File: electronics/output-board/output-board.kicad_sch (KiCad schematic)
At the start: 27 parts, among them J14 Arming switch, J19 Extra IO, J3 12V In, J4 Conn_01x02, J5 SWD Header, J6 Conn_01x02, SW1 SW_Push_Dual, U1 MAX33012EASA+, U2 LD3985M33R_SOT23, U3 STM32F105VBH6, Y1 25MHz 9pF

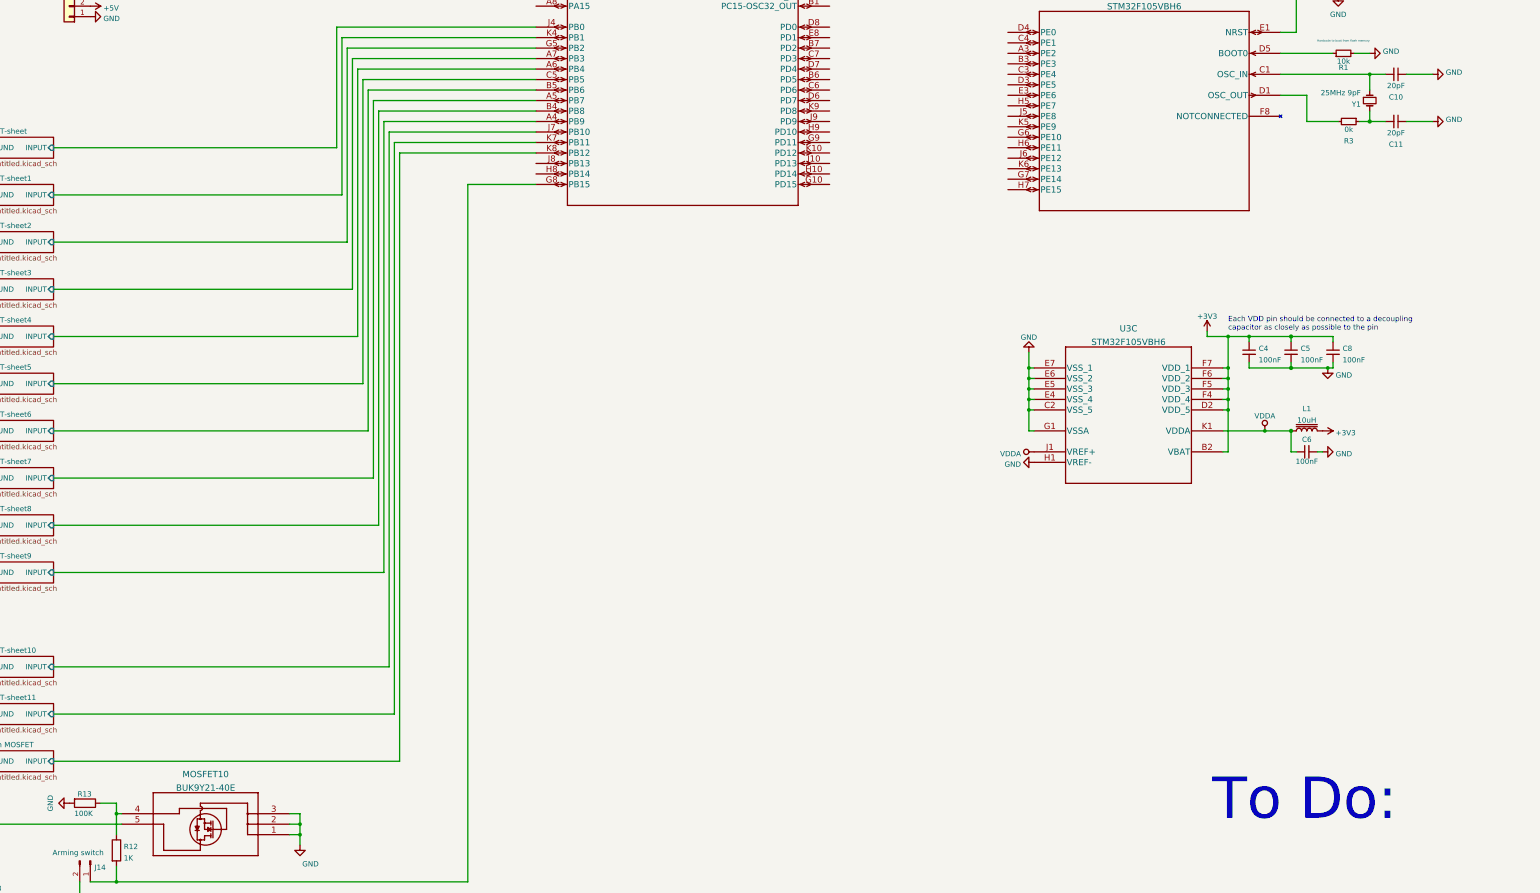
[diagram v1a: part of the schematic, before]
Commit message: continued working on four-layer output board
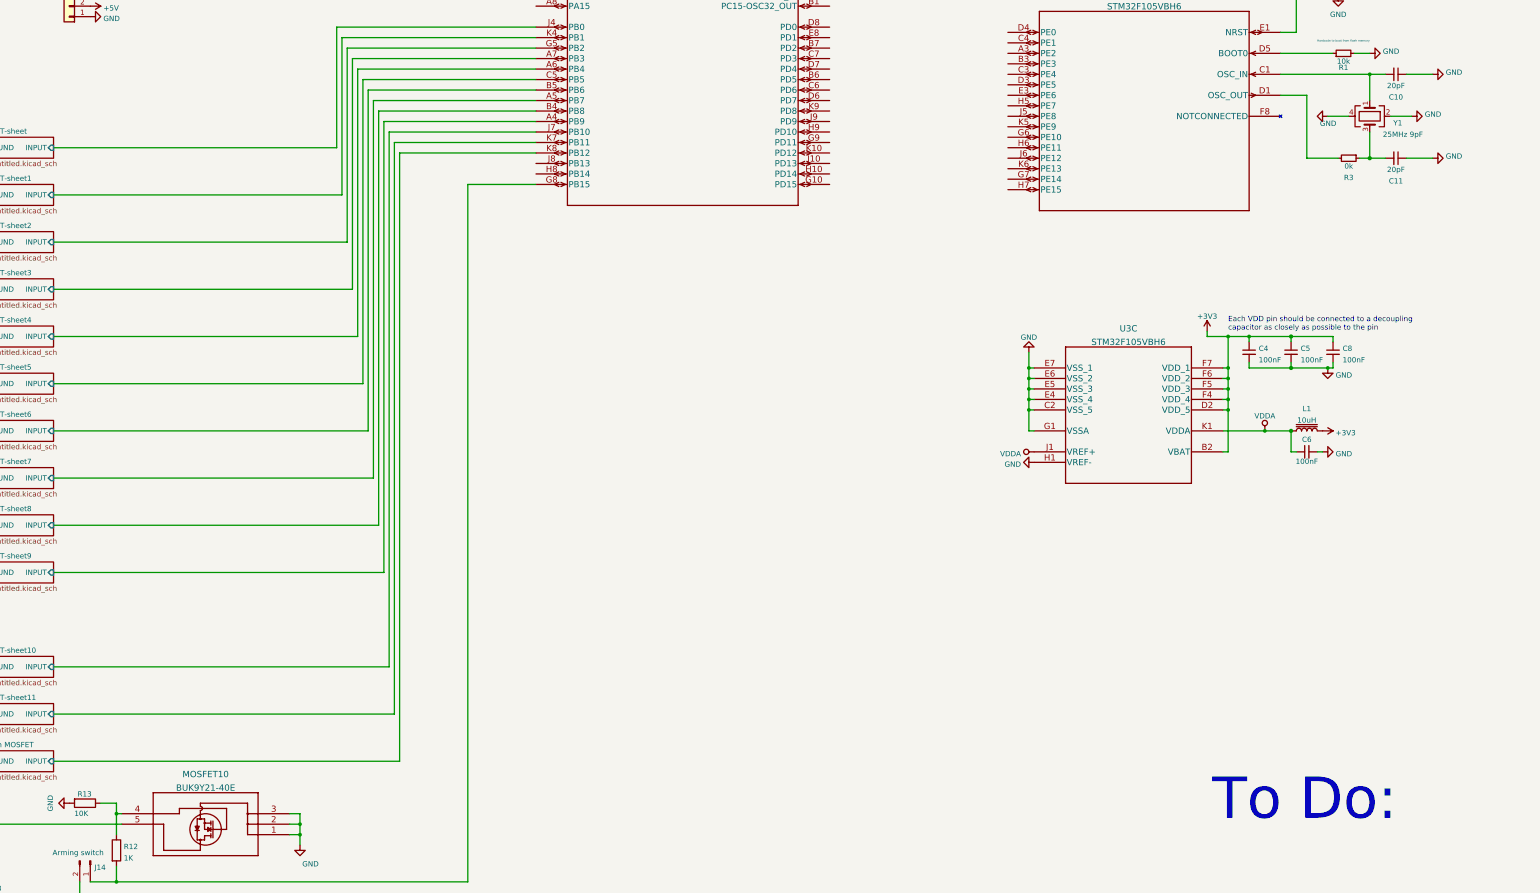
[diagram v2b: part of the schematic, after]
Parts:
- removed Y1: 25MHz 9pF, symbol Device:Crystal_Small
- added Y1: 25MHz 9pF, Crystal:Crystal_SMD_3225-4Pin_3.2x2.5mm, symbol Device:Crystal_GND24
- R13: value 100K -> 10K
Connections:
- net GND: now also Y1.2, Y1.4
- net at C10.2, U3.C1 (OSC_IN): now also Y1.1
- net at C11.2, R3.1: now also Y1.3
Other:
- moved on the sheet: C11, R3

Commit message: finished (mostly) output board
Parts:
- added C12, C13, C9: 100nF, Capacitor_SMD:C_0603_1608Metric, symbol Device:C_Small
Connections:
- net +3V3: now also C12.1, C13.1, C9.1
- net GND: now also C12.2, C13.2, C9.2
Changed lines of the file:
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@@
   (junction (at 349.25 101.6) (diameter 1.016) (color 0 0 0 0))
   (junction (at 356.87 194.31) (diameter 0) (color 0 0 0 0))
+  (junction (at 358.14 186.69) (diameter 0) (color 0 0 0 0))
+  (junction (at 358.14 194.31) (diameter 0) (color 0 0 0 0))
   (junction (at 359.41 97.79) (diameter 0) (color 0 0 0 0))
   (junction (at 359.41 101.6) (diameter 0) (color 0 0 0 0))
   (junction (at 367.03 123.19) (diameter 0) (color 0 0 0 0))
   (junction (at 367.03 143.51) (diameter 1.016) (color 0 0 0 0))
+  (junction (at 368.3 186.69) (diameter 0) (color 0 0 0 0))
+  (junction (at 368.3 194.31) (diameter 0) (color 0 0 0 0))
+  (junction (at 378.46 186.69) (diameter 0) (color 0 0 0 0))
+  (junction (at 378.46 194.31) (diameter 0) (color 0 0 0 0))
   (wire (pts (xy 25.4 81.28) (xy 35.56 81.28))
     (stroke (width 0) (type solid) (color 0 0 0 0))
@@
     (stroke (width 0) (type solid) (color 0 0 0 0))
   )
+  (wire (pts (xy 358.14 186.69) (xy 368.3 186.69))
+    (stroke (width 0) (type default) (color 0 0 0 0))
+  )
   (wire (pts (xy 358.14 193.04) (xy 358.14 194.31))
     (stroke (width 0) (type solid) (color 0 0 0 0))
   )
+  (wire (pts (xy 358.14 194.31) (xy 368.3 194.31))
+    (stroke (width 0) (type default) (color 0 0 0 0))
+  )
   (wire (pts (xy 359.41 92.71) (xy 359.41 97.79))
     (stroke (width 0) (type default) (color 0 0 0 0))
@@
     (stroke (width 0) (type solid) (color 0 0 0 0))
   )
+  (wire (pts (xy 368.3 186.69) (xy 368.3 187.96))
+    (stroke (width 0) (type default) (color 0 0 0 0))
+  )
+  (wire (pts (xy 368.3 186.69) (xy 378.46 186.69))
+    (stroke (width 0) (type default) (color 0 0 0 0))
+  )
+  (wire (pts (xy 368.3 193.04) (xy 368.3 194.31))
+    (stroke (width 0) (type default) (color 0 0 0 0))
+  )
+  (wire (pts (xy 368.3 194.31) (xy 378.46 194.31))
+    (stroke (width 0) (type default) (color 0 0 0 0))
+  )
   (wire (pts (xy 370.84 123.19) (xy 367.03 123.19))
     (stroke (width 0) (type solid) (color 0 0 0 0))
@@
     (stroke (width 0) (type default) (color 0 0 0 0))
   )
+  (wire (pts (xy 378.46 186.69) (xy 378.46 187.96))
+    (stroke (width 0) (type default) (color 0 0 0 0))
+  )
+  (wire (pts (xy 378.46 186.69) (xy 388.62 186.69))
+    (stroke (width 0) (type default) (color 0 0 0 0))
+  )
+  (wire (pts (xy 378.46 193.04) (xy 378.46 194.31))
+    (stroke (width 0) (type default) (color 0 0 0 0))
+  )
+  (wire (pts (xy 378.46 194.31) (xy 388.62 194.31))
+    (stroke (width 0) (type default) (color 0 0 0 0))
+  )
   (wire (pts (xy 382.27 123.19) (xy 375.92 123.19))
     (stroke (width 0) (type solid) (color 0 0 0 0))
@@
   (wire (pts (xy 382.27 143.51) (xy 375.92 143.51))
     (stroke (width 0) (type solid) (color 0 0 0 0))
+  )
+  (wire (pts (xy 388.62 187.96) (xy 388.62 186.69))
+    (stroke (width 0) (type default) (color 0 0 0 0))
+  )
+  (wire (pts (xy 388.62 193.04) (xy 388.62 194.31))
+    (stroke (width 0) (type default) (color 0 0 0 0))
   )
   (text "To Do:\n\n-Find MCU\n-Add IO Breakout\n-Finalize Connectors\n-Put together final parrts list\n-Buy parts and board"
@@
     (pin "2")
   )
+  (symbol (lib_id "Device:C_Small") (at 368.3 190.5 0) (unit 1)
+    (in_bom yes) (on_board yes) (fields_autoplaced)
+    (property "Reference" "C9" (id 0) (at 370.6242 189.5915 0)
+      (effects (font (size 1.27 1.27)) (justify left))
+    )
+    (property "Value" "100nF" (id 1) (at 370.6242 192.3666 0)
+      (effects (font (size 1.27 1.27)) (justify left))
+    )
+    (property "Footprint" "Capacitor_SMD:C_0603_1608Metric" (id 2) (at 368.3 190.5 0)
+      (effects (font (size 1.27 1.27)) hide)
+    )
+    (property "Datasheet" "~" (id 3) (at 368.3 190.5 0)
+      (effects (font (size 1.27 1.27)) hide)
+    )
+    (pin "1")
+    (pin "2")
+  )
   (symbol (lib_id "Device:C_Small") (at 373.38 123.19 270) (unit 1)
     (in_bom yes) (on_board yes) (fields_autoplaced)
@@
     )
     (property "Datasheet" "~" (id 3) (at 373.38 143.51 0)
+      (effects (font (size 1.27 1.27)) hide)
+    )
+    (pin "1")
+    (pin "2")
+  )
+  (symbol (lib_id "Device:C_Small") (at 378.46 190.5 0) (unit 1)
+    (in_bom yes) (on_board yes) (fields_autoplaced)
+    (property "Reference" "C12" (id 0) (at 380.7842 189.5915 0)
+      (effects (font (size 1.27 1.27)) (justify left))
+    )
+    (property "Value" "100nF" (id 1) (at 380.7842 192.3666 0)
+      (effects (font (size 1.27 1.27)) (justify left))
+    )
+    (property "Footprint" "Capacitor_SMD:C_0603_1608Metric" (id 2) (at 378.46 190.5 0)
+      (effects (font (size 1.27 1.27)) hide)
+    )
+    (property "Datasheet" "~" (id 3) (at 378.46 190.5 0)
+      (effects (font (size 1.27 1.27)) hide)
+    )
+    (pin "1")
+    (pin "2")
+  )
+  (symbol (lib_id "Device:C_Small") (at 388.62 190.5 0) (unit 1)
+    (in_bom yes) (on_board yes) (fields_autoplaced)
+    (property "Reference" "C13" (id 0) (at 390.9442 189.5915 0)
+      (effects (font (size 1.27 1.27)) (justify left))
+    )
+    (property "Value" "100nF" (id 1) (at 390.9442 192.3666 0)
+      (effects (font (size 1.27 1.27)) (justify left))
+    )
+    (property "Footprint" "Capacitor_SMD:C_0603_1608Metric" (id 2) (at 388.62 190.5 0)
+      (effects (font (size 1.27 1.27)) hide)
+    )
+    (property "Datasheet" "~" (id 3) (at 388.62 190.5 0)
       (effects (font (size 1.27 1.27)) hide)
     )
@@
       (reference "C8") (unit 1) (value "100nF") (footprint "Capacitor_SMD:C_0603_1608Metric")
     )
+    (path "/010ef4f4-9f94-484c-9897-7c6ce78e9c4e"
+      (reference "C9") (unit 1) (value "100nF") (footprint "Capacitor_SMD:C_0603_1608Metric")
+    )
     (path "/a4541931-eddb-411e-a18a-57712146f98f"
       (reference "C10") (unit 1) (value "20pF") (footprint "Capacitor_SMD:C_0603_1608Metric")
@@
       (reference "C11") (unit 1) (value "20pF") (footprint "Capacitor_SMD:C_0603_1608Metric")
     )
+    (path "/6cd2130a-c637-408d-a088-250286f21823"
+      (reference "C12") (unit 1) (value "100nF") (footprint "Capacitor_SMD:C_0603_1608Metric")
+    )
+    (path "/6e02d979-cfcd-4273-9c44-85a61a10a0a0"
+      (reference "C13") (unit 1) (value "100nF") (footprint "Capacitor_SMD:C_0603_1608Metric")
+    )
     (path "/36b6bf08-79b4-4cbd-9663-410f8ea161a3/fdaba974-f779-4819-9be4-c0a4f95a2d0b"

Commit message: minor changes to output board
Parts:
- added D?: POWER LED, LED_SMD:LED_1206_3216Metric, symbol Device:LED
- added J?: Ignition Detector, CustomFootprints:PowerPoleThroughHole, symbol Connector:Conn_01x02_Male
- added R?: 500, Resistor_SMD:R_0603_1608Metric, symbol Device:R
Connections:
- net +12V: now also R?.1
- net GND: now also J19.1 (Pin_1), D?.1 (K), J?.1 (Pin_1)
- net at U3.H2 (PA1): now also J?.2 (Pin_2); no longer J19.1 (Pin_1)
- new net: D?.2 (A), R?.2
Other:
- note removed: "To Do: -Find MCU -Add IO Breakout -Finalize Connectors -Put together final parrts list -Buy parts and board"
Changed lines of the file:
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@@
     (stroke (width 0) (type solid) (color 0 0 0 0))
+  )
+  (wire (pts (xy 53.34 350.52) (xy 64.77 350.52))
+    (stroke (width 0) (type default) (color 0 0 0 0))
+  )
+  (wire (pts (xy 53.34 356.87) (xy 60.96 356.87))
+    (stroke (width 0) (type default) (color 0 0 0 0))
   )
   (wire (pts (xy 54.61 318.77) (xy 54.61 322.58))
@@
     (stroke (width 0) (type default) (color 0 0 0 0))
   )
+  (wire (pts (xy 68.58 356.87) (xy 73.66 356.87))
+    (stroke (width 0) (type default) (color 0 0 0 0))
+  )
   (wire (pts (xy 69.85 45.72) (xy 69.85 48.26))
     (stroke (width 0) (type solid) (color 0 0 0 0))
@@
     (stroke (width 0) (type solid) (color 0 0 0 0))
   )
+  (wire (pts (xy 72.39 350.52) (xy 73.66 350.52))
+    (stroke (width 0) (type default) (color 0 0 0 0))
+  )
+  (wire (pts (xy 73.66 350.52) (xy 73.66 356.87))
+    (stroke (width 0) (type default) (color 0 0 0 0))
+  )
   (wire (pts (xy 76.2 78.74) (xy 85.09 78.74))
     (stroke (width 0) (type solid) (color 0 0 0 0))
@@
     (stroke (width 0) (type default) (color 0 0 0 0))
   )
-  (wire (pts (xy 135.89 71.12) (xy 165.1 71.12))
+  (wire (pts (xy 135.89 71.12) (xy 138.43 71.12))
     (stroke (width 0) (type default) (color 0 0 0 0))
   )
@@
     (stroke (width 0) (type default) (color 0 0 0 0))
   )
+  (wire (pts (xy 152.4 71.12) (xy 152.4 60.96))
+    (stroke (width 0) (type default) (color 0 0 0 0))
+  )
+  (wire (pts (xy 154.94 60.96) (xy 154.94 63.5))
+    (stroke (width 0) (type default) (color 0 0 0 0))
+  )
+  (wire (pts (xy 154.94 63.5) (xy 156.21 63.5))
+    (stroke (width 0) (type default) (color 0 0 0 0))
+  )
   (wire (pts (xy 157.48 83.82) (xy 135.89 83.82))
     (stroke (width 0) (type default) (color 0 0 0 0))
@@
     (stroke (width 0) (type default) (color 0 0 0 0))
   )
+  (wire (pts (xy 165.1 71.12) (xy 152.4 71.12))
+    (stroke (width 0) (type default) (color 0 0 0 0))
+  )
   (wire (pts (xy 165.1 81.28) (xy 162.56 81.28))
     (stroke (width 0) (type default) (color 0 0 0 0))
@@
   (wire (pts (xy 388.62 193.04) (xy 388.62 194.31))
     (stroke (width 0) (type default) (color 0 0 0 0))
-  )
-  (text "To Do:\n\n-Find MCU\n-Add IO Breakout\n-Finalize Connectors\n-Put together final parrts list\n-Buy parts and board"
-    (at 328.93 401.32 0)
-    (effects (font (size 10 10)) (justify left bottom))
   )
   (text "Each VDD pin should be connected to a decoupling\ncapacitor as closely as possible to the pin"
@@
     (pin "1")
   )
+  (symbol (lib_id "power:+12V") (at 53.34 350.52 90) (unit 1)
+    (in_bom yes) (on_board yes)
+    (property "Reference" "#PWR?" (id 0) (at 57.15 350.52 0)
+      (effects (font (size 1.27 1.27)) hide)
+    )
+    (property "Value" "+12V" (id 1) (at 47.5074 350.52 90))
+    (property "Footprint" "" (id 2) (at 53.34 350.52 0)
+      (effects (font (size 1.27 1.27)) hide)
+    )
+    (property "Datasheet" "" (id 3) (at 53.34 350.52 0)
+      (effects (font (size 1.27 1.27)) hide)
+    )
+    (pin "1")
+  )
   (symbol (lib_id "power:+5V") (at 54.61 322.58 180) (unit 1)
     (in_bom yes) (on_board yes) (fields_autoplaced)
@@
     (pin "1")
   )
+  (symbol (lib_id "power:GND") (at 53.34 356.87 270) (unit 1)
+    (in_bom yes) (on_board yes)
+    (property "Reference" "#PWR?" (id 0) (at 46.99 356.87 0)
+      (effects (font (size 1.27 1.27)) hide)
+    )
+    (property "Value" "GND" (id 1) (at 47.5074 356.87 90))
+    (property "Footprint" "" (id 2) (at 53.34 356.87 0)
+      (effects (font (size 1.27 1.27)) hide)
+    )
+    (property "Datasheet" "" (id 3) (at 53.34 356.87 0)
+      (effects (font (size 1.27 1.27)) hide)
+    )
+    (pin "1")
+  )
   (symbol (lib_id "power:GND") (at 57.15 109.22 90) (unit 1)
     (in_bom yes) (on_board yes) (fields_autoplaced)
@@
     )
     (property "Datasheet" "" (id 3) (at 107.95 309.88 0)
+      (effects (font (size 1.27 1.27)) hide)
+    )
+    (pin "1")
+  )
+  (symbol (lib_id "power:GND") (at 138.43 71.12 90) (unit 1)
+    (in_bom yes) (on_board yes) (fields_autoplaced)
+    (property "Reference" "#PWR?" (id 0) (at 144.78 71.12 0)
+      (effects (font (size 1.27 1.27)) hide)
+    )
+    (property "Value" "GND" (id 1) (at 141.6051 71.599 90)
+      (effects (font (size 1.27 1.27)) (justify right))
+    )
+    (property "Footprint" "" (id 2) (at 138.43 71.12 0)
+      (effects (font (size 1.27 1.27)) hide)
+    )
+    (property "Datasheet" "" (id 3) (at 138.43 71.12 0)
+      (effects (font (size 1.27 1.27)) hide)
+    )
+    (pin "1")
+  )
+  (symbol (lib_id "power:GND") (at 156.21 63.5 90) (unit 1)
+    (in_bom yes) (on_board yes) (fields_autoplaced)
+    (property "Reference" "#PWR?" (id 0) (at 162.56 63.5 0)
+      (effects (font (size 1.27 1.27)) hide)
+    )
+    (property "Value" "GND" (id 1) (at 159.3851 63.979 90)
+      (effects (font (size 1.27 1.27)) (justify right))
+    )
+    (property "Footprint" "" (id 2) (at 156.21 63.5 0)
+      (effects (font (size 1.27 1.27)) hide)
+    )
+    (property "Datasheet" "" (id 3) (at 156.21 63.5 0)
       (effects (font (size 1.27 1.27)) hide)
     )
@@
     (pin "2")
   )
+  (symbol (lib_id "Connector:Conn_01x02_Male") (at 154.94 55.88 270) (unit 1)
+    (in_bom yes) (on_board yes)
+    (property "Reference" "J?" (id 0) (at 155.9561 57.4734 90)
+      (effects (font (size 1.27 1.27)) (justify left))
+    )
+    (property "Value" "Ignition Detector" (id 1) (at 147.0661 53.8985 90)
+      (effects (font (size 1.27 1.27)) (justify left))
+    )
+    (property "Footprint" "CustomFootprints:PowerPoleThroughHole" (id 2) (at 154.94 55.88 0)
+      (effects (font (size 1.27 1.27)) hide)
+    )
+    (property "Datasheet" "~" (id 3) (at 154.94 55.88 0)
+      (effects (font (size 1.27 1.27)) hide)
+    )
+    (pin "1")
+    (pin "2")
+  )
   (symbol (lib_id "Device:C_Small") (at 36.83 50.8 0) (unit 1)
     (in_bom yes) (on_board yes) (fields_autoplaced)
@@
     )
     (property "Datasheet" "~" (id 3) (at 63.5 311.15 0)
+      (effects (font (size 1.27 1.27)) hide)
+    )
+    (pin "1")
+    (pin "2")
+  )
+  (symbol (lib_id "Device:R") (at 68.58 350.52 90) (unit 1)
+    (in_bom yes) (on_board yes)
+    (property "Reference" "R?" (id 0) (at 68.58 348.0774 90))
+    (property "Value" "500" (id 1) (at 68.6275 350.6319 90))
+    (property "Footprint" "Resistor_SMD:R_0603_1608Metric" (id 2) (at 68.58 352.298 90)
+      (effects (font (size 1.27 1.27)) hide)
+    )
+    (property "Datasheet" "~" (id 3) (at 68.58 350.52 0)
+      (effects (font (size 1.27 1.27)) hide)
+    )
+    (pin "1")
+    (pin "2")
+  )
+  (symbol (lib_id "Device:LED") (at 64.77 356.87 0) (unit 1)
+    (in_bom yes) (on_board yes) (fields_autoplaced)
+    (property "Reference" "D?" (id 0) (at 64.389 351.6334 0))
+    (property "Value" "POWER LED" (id 1) (at 64.389 354.4085 0))
+    (property "Footprint" "LED_SMD:LED_1206_3216Metric" (id 2) (at 64.77 356.87 0)
+      (effects (font (size 1.27 1.27)) hide)
+    )
+    (property "Datasheet" "~" (id 3) (at 64.77 356.87 0)
       (effects (font (size 1.27 1.27)) hide)
     )
@@
       (reference "#PWR0144") (unit 1) (value "+12V") (footprint "")
     )
+    (path "/0d22df0e-0fce-4231-9dd1-002b9c289430"
+      (reference "#PWR?") (unit 1) (value "GND") (footprint "")
+    )
+    (path "/3b97f976-e2c2-46d6-92c9-63c2a4bf9ffe"
+      (reference "#PWR?") (unit 1) (value "GND") (footprint "")
+    )
+    (path "/f01eb261-9640-4b48-9a5e-239027884851"
+      (reference "#PWR?") (unit 1) (value "+12V") (footprint "")
+    )
+    (path "/fd3f52cc-6c59-4511-9709-ca40718f93e3"
+      (reference "#PWR?") (unit 1) (value "GND") (footprint "")
+    )
     (path "/2c82cb5d-5242-4074-b9d4-e6795eb314a0"
       (reference "C1") (unit 1) (value "1uF") (footprint "Capacitor_SMD:C_0603_1608Metric")
@@
       (reference "D13") (unit 1) (value "LED") (footprint "LED_SMD:LED_1206_3216Metric")
     )
+    (path "/4783b386-783a-41d6-9291-46521936e904"
+      (reference "D?") (unit 1) (value "POWER LED") (footprint "LED_SMD:LED_1206_3216Metric")
+    )
     (path "/36b6bf08-79b4-4cbd-9663-410f8ea161a3/6b60855c-5bd9-463e-a130-45a0cde73160"
       (reference "J1") (unit 1) (value "Conn_01x02_Male") (footprint "CustomFootprints:LatchingConnector2POS")
@@
       (reference "J19") (unit 1) (value "Extra IO") (footprint "Connector_PinHeader_2.54mm:PinHeader_2x03_P2.54mm_Vertical")
     )
+    (path "/e75c763c-ea07-4fb0-adb6-c7bc181ebd48"
+      (reference "J?") (unit 1) (value "Ignition Detector") (footprint "CustomFootprints:PowerPoleThroughHole")
+    )
     (path "/732556df-c8ec-474a-b66b-6a4645edf50b"
       (reference "L1") (unit 1) (value "10uH") (footprint "Inductor_SMD:L_0603_1608Metric")
@@
       (reference "R30") (unit 1) (value "500") (footprint "Resistor_SMD:R_0603_1608Metric")
     )
+    (path "/5e354459-5766-4858-a84d-614f7dc35afb"
+      (reference "R?") (unit 1) (value "500") (footprint "Resistor_SMD:R_0603_1608Metric")
+    )
     (path "/5a984209-2501-4b3c-984e-c60f26a02fd0"
